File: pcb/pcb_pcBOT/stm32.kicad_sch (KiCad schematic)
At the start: 16 parts, among them J301 ST_link, SW301 Reset_Button, U301 LD3985M33R_SOT23, U303 STM32G431KBT6

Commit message: avancement des schematics
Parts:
- renumbered C308 to C305, C309 to C306, C305 to C307, C306 to C308, C307 to C309, U303 to U301, U301 to U302
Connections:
- net IMU_INT1: now reaches U301.13 (PB0)
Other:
- company: (none) -> ENSEA G5
- title: (none) -> STM32_PcBOT

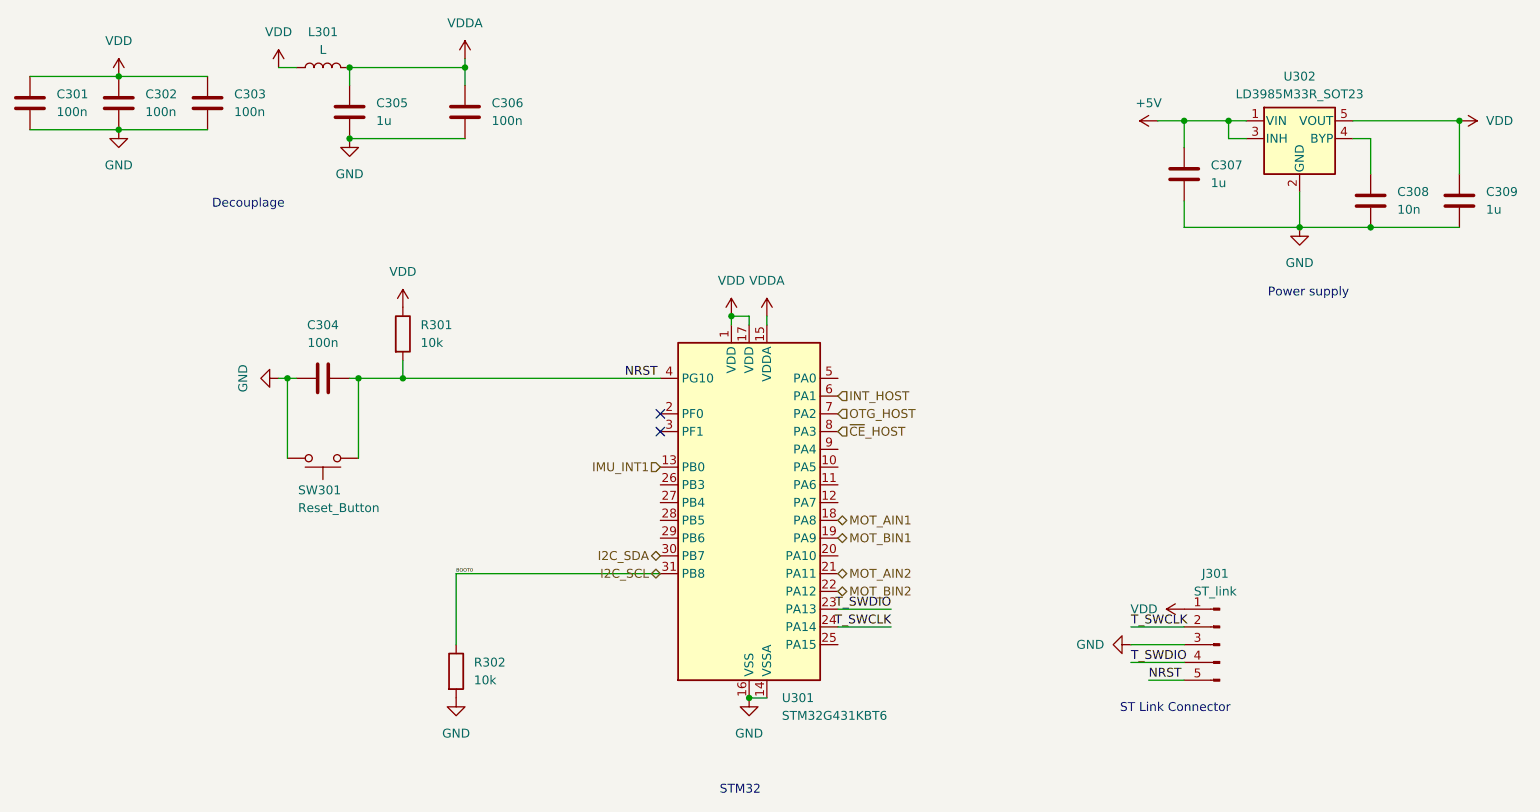
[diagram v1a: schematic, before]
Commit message: ajout du module nrf + petites corrections
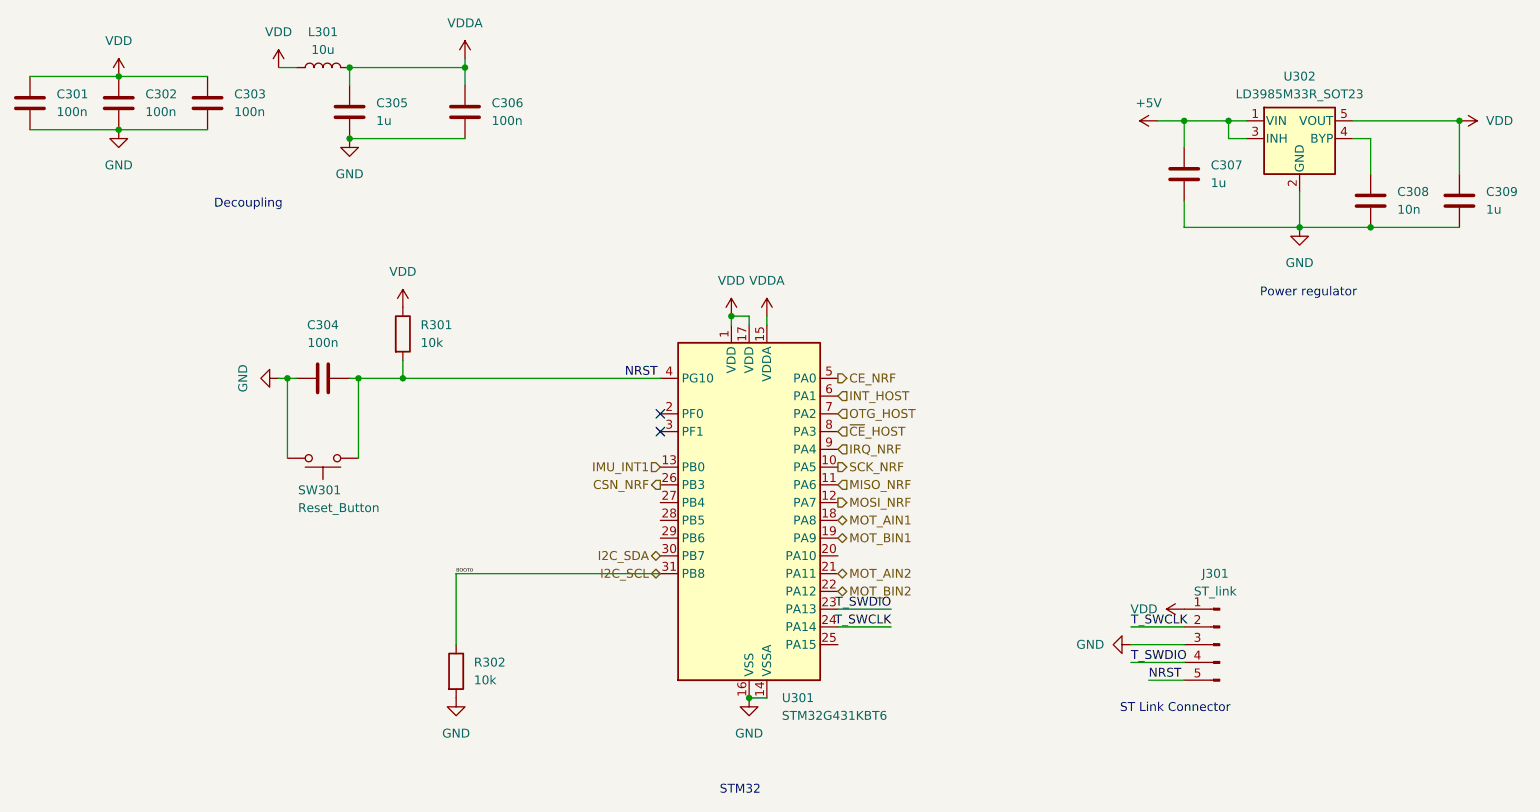
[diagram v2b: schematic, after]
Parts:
- L301: value L -> 10u
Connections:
- net SCK_NRF: now reaches U301.10 (PA5)
- net MISO_NRF: now reaches U301.11 (PA6)
- net MOSI_NRF: now reaches U301.12 (PA7)
- net CSN_NRF: now reaches U301.26 (PB3)
- net CE_NRF: now reaches U301.5 (PA0)
- net IRQ_NRF: now reaches U301.9 (PA4)
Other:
- note added: "Decoupling"
- note added: "Power regulator"
- note removed: "Decouplage"
- note removed: "Power supply"
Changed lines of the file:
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@@
 		)
 	)
-	(text "Decouplage\n"
+	(text "Decoupling\n"
 		(exclude_from_sim no)
 		(at 65.532 56.388 0)
@@
 		)
 	)
-	(text "Power supply\n"
+	(text "Power regulator\n\n\n"
 		(exclude_from_sim no)
-		(at 217.17 69.088 0)
+		(at 217.17 71.12 0)
 		(effects
 			(font
@@
 		)
 	)
+	(hierarchical_label "MISO_NRF"
+		(shape input)
+		(at 149.86 96.52 0)
+		(effects
+			(font
+				(size 1.27 1.27)
+			)
+			(justify left)
+		)
+	)
 	(hierarchical_label "MOT_BIN2"
 		(shape bidirectional)
@@
 		)
 	)
+	(hierarchical_label "CSN_NRF"
+		(shape output)
+		(at 124.46 96.52 180)
+		(effects
+			(font
+				(size 1.27 1.27)
+			)
+			(justify right)
+		)
+	)
 	(hierarchical_label "INT_HOST"
 		(shape input)
@@
 		)
 	)
+	(hierarchical_label "SCK_NRF"
+		(shape output)
+		(at 149.86 93.98 0)
+		(effects
+			(font
+				(size 1.27 1.27)
+			)
+			(justify left)
+		)
+	)
 	(hierarchical_label "~{CE}_HOST"
 		(shape input)
@@
 		)
 	)
+	(hierarchical_label "MOSI_NRF"
+		(shape output)
+		(at 149.86 99.06 0)
+		(effects
+			(font
+				(size 1.27 1.27)
+			)
+			(justify left)
+		)
+	)
 	(hierarchical_label "MOT_AIN1"
 		(shape bidirectional)
@@
 			)
 			(justify right)
+		)
+	)
+	(hierarchical_label "CE_NRF"
+		(shape output)
+		(at 149.86 81.28 0)
+		(effects
+			(font
+				(size 1.27 1.27)
+			)
+			(justify left)
+		)
+	)
+	(hierarchical_label "IRQ_NRF"
+		(shape input)
+		(at 149.86 91.44 0)
+		(effects
+			(font
+				(size 1.27 1.27)
+			)
+			(justify left)
 		)
 	)
@@
 			)
 		)
-		(property "Value" "L"
+		(property "Value" "10u"
 			(at 76.2 34.29 90)
 			(effects

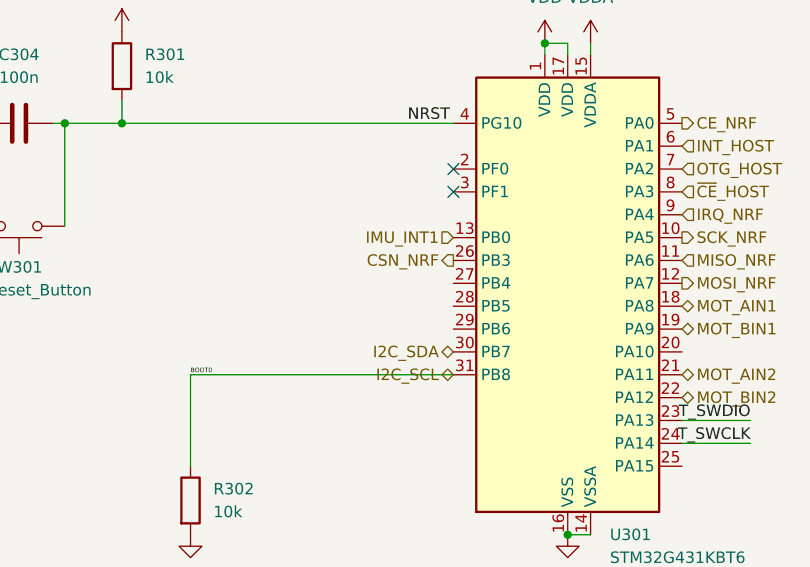
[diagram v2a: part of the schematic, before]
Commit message: complement tof et connections, mise a jour du firmware
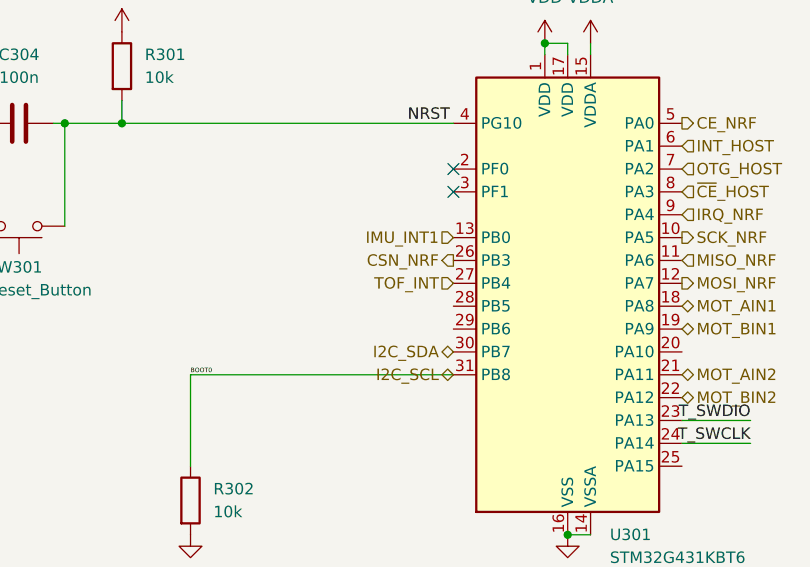
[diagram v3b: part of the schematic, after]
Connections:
- net TOF_INT: now reaches U301.27 (PB4)
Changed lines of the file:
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@@
+		)
+	)
+	(hierarchical_label "TOF_INT"
+		(shape input)
+		(at 124.46 99.06 180)
+		(effects
+			(font
+				(size 1.27 1.27)
+			)
+			(justify right)
 		)
 	)

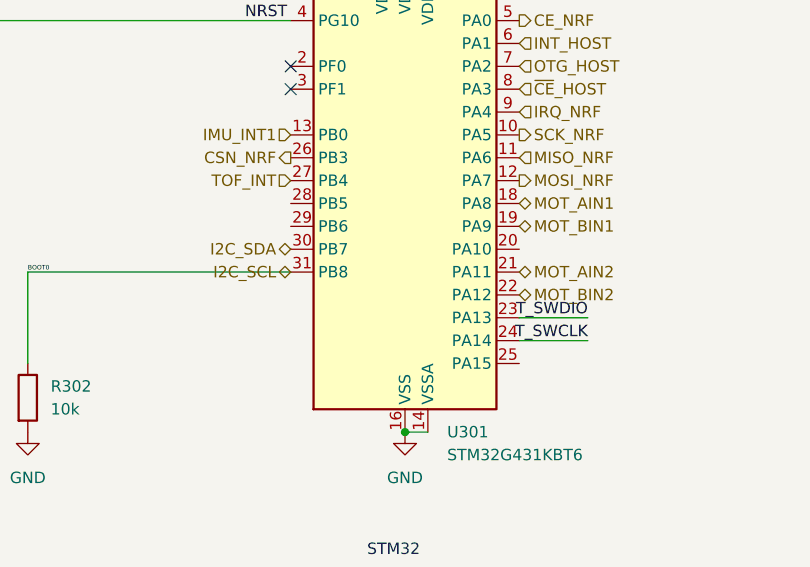
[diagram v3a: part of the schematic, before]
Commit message: corrections d'erreurs et liasons bus i2c et spi
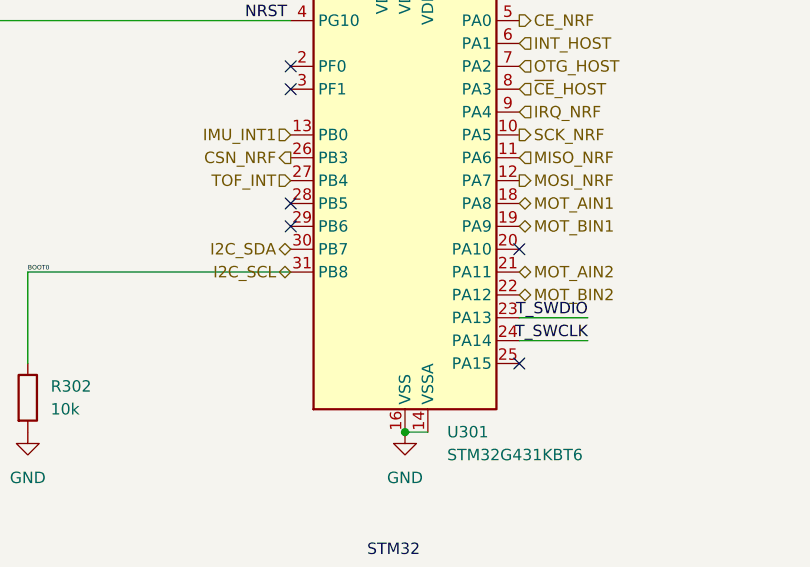
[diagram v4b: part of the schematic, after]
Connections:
- no-connect marks 2 -> 6
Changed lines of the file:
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@@
+	)
+	(no_connect
+		(at 149.86 119.38)
+	)
+	(no_connect
+		(at 149.86 106.68)
+	)
+	(no_connect
+		(at 124.46 101.6)
 	)
 	(no_connect
@@
 		(at 124.46 86.36)
 	)
+	(no_connect
+		(at 124.46 104.14)
+	)
 	(wire

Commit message: Ajout empreintes (incomplet) + test erc correct
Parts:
- removed C308: 10n, symbol Device:C
- removed U302: LD3985M33R_SOT23, Package_TO_SOT_SMD:SOT-23-5, symbol Regulator_Linear:LD3985M33R_SOT23
- added U303: BU33??, Package_TO_SOT_SMD:TSOT-23-5, symbol Regulator_Linear:MIC5365-3.3YD5
- C301, C302, C303, C304, C305, C306, C307, C309: footprint (none) -> Capacitor_SMD:C_0805_2012Metric_Pad1.18x1.45mm_HandSolder
- J301: footprint (none) -> Connector_PinHeader_1.27mm:PinHeader_2x07_P1.27mm_Vertical_SMD
- L301: footprint (none) -> Inductor_SMD:L_0805_2012Metric_Pad1.05x1.20mm_HandSolder
- R301, R302: footprint (none) -> Resistor_SMD:R_0805_2012Metric_Pad1.20x1.40mm_HandSolder
- SW301: footprint (none) -> Button_Switch_THT:SW_PUSH_6mm
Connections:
- net +5V: now also U303.1 (VIN), U303.3 (EN)
- net GND: now also U303.2 (GND)
- net VDD: now also U303.5 (VOUT)
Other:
- moved on the sheet: C307, C309

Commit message: Revert "Ajout empreintes (incomplet) + test erc correct"
This reverts commit 267ed5519d67c336b99c9c80b0ac2067182b82a3.
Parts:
- removed U303: BU33??, Package_TO_SOT_SMD:TSOT-23-5, symbol Regulator_Linear:MIC5365-3.3YD5
- added C308: 10n, symbol Device:C
- added U302: LD3985M33R_SOT23, Package_TO_SOT_SMD:SOT-23-5, symbol Regulator_Linear:LD3985M33R_SOT23
- C301, C302, C303, C304, C305, C306, C307, C309: footprint Capacitor_SMD:C_0805_2012Metric_Pad1.18x1.45mm_HandSolder -> (none)
- J301: footprint Connector_PinHeader_1.27mm:PinHeader_2x07_P1.27mm_Vertical_SMD -> (none)
- L301: footprint Inductor_SMD:L_0805_2012Metric_Pad1.05x1.20mm_HandSolder -> (none)
- R301, R302: footprint Resistor_SMD:R_0805_2012Metric_Pad1.20x1.40mm_HandSolder -> (none)
- SW301: footprint Button_Switch_THT:SW_PUSH_6mm -> (none)
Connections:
- net +5V: now also U302.1 (VIN), U302.3 (INH)
- net GND: now also C308.2, U302.2 (GND)
- net VDD: now also U302.5 (VOUT)
- new net: C308.1, U302.4 (BYP)
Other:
- moved on the sheet: C307, C309
